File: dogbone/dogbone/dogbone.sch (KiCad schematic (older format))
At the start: 11 parts, among them J1 jstsh4x1, U1 TLV2771CDBVT

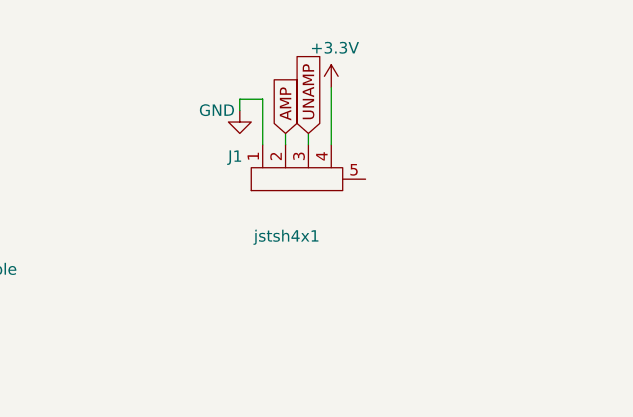
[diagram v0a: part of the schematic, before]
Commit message: added grbl files for dogbone, and update csv
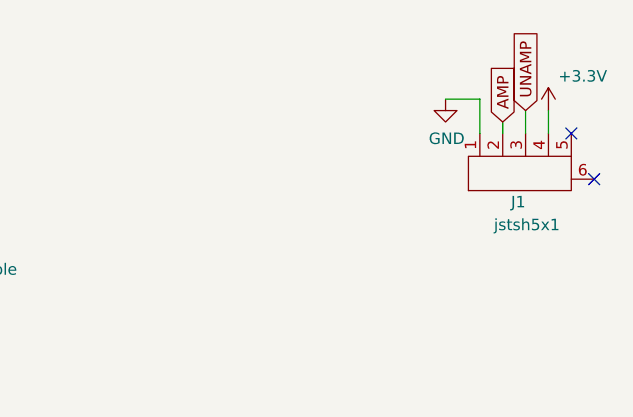
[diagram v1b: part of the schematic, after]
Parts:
- removed J1: jstsh4x1, exocam_charge_amp:jstsh4x1, symbol exocam_charge_amp:jstsh4x1
- added J1: jstsh5x1, symbol exocam_charge_amp:jstsh5x1
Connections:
- net +3V3: now also J1.4
- net AMP: now also J1.2
- net GND: now also J1.1
- net UNAMP: now also J1.3
- no-connect marks 0 -> 2
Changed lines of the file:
@@
 UNAMP
 $Comp
-L exocam_charge_amp:jstsh4x1 J1
-U 1 1 60E73D05
-P 4800 1050
-F 0 "J1" V 4849 1088 50  0000 L CNN
-F 1 "jstsh4x1" V 4500 750 50  0000 L CNN
-F 2 "exocam_charge_amp:jstsh4x1" H 4750 1200 50  0001 C CNN
-F 3 "" H 4750 1200 50  0001 C CNN
-	1    4800 1050
+L exocam_charge_amp:jstsh5x1 J1
+U 1 1 60F622D2
+P 5750 1000
+F 0 "J1" V 5550 750 50  0000 L CNN
+F 1 "jstsh5x1" V 5450 600 50  0000 L CNN
+F 2 "" H 5700 1150 50  0001 C CNN
+F 3 "" H 5700 1150 50  0001 C CNN
+	1    5750 1000
 	0    -1   -1   0
 $EndComp
 $Comp
-L power:GND #PWR0105
-U 1 1 60E75791
-P 4750 800
-F 0 "#PWR0105" H 4750 550 50  0001 C CNN
-F 1 "GND" H 4650 800 50  0000 C CNN
-F 2 "" H 4750 800 50  0001 C CNN
-F 3 "" H 4750 800 50  0001 C CNN
-	1    4750 800
+L exocam_charge_amp-cache:+3.3V #PWR?
+U 1 1 60F62E23
+P 6100 800
+F 0 "#PWR?" H 6100 650 50  0001 C CNN
+F 1 "+3.3V" H 6250 950 50  0000 C CNN
+F 2 "" H 6100 800 50  0001 C CNN
+F 3 "" H 6100 800 50  0001 C CNN
+	1    6100 800
 	1    0    0    -1
 $EndComp
-Wire Wire Line
-	4750 750  4750 800
-Wire Wire Line
-	4750 750  4850 750
-Wire Wire Line
-	4850 750  4850 950
 $Comp
-L exocam_charge_amp-cache:+3.3V #PWR0106
-U 1 1 60E76333
-P 5150 700
-F 0 "#PWR0106" H 5150 550 50  0001 C CNN
-F 1 "+3.3V" H 5165 873 50  0000 C CNN
-F 2 "" H 5150 700 50  0001 C CNN
-F 3 "" H 5150 700 50  0001 C CNN
-	1    5150 700
+L power:GND #PWR?
+U 1 1 60F633AB
+P 5650 750
+F 0 "#PWR?" H 5650 500 50  0001 C CNN
+F 1 "GND" H 5655 577 50  0000 C CNN
+F 2 "" H 5650 750 50  0001 C CNN
+F 3 "" H 5650 750 50  0001 C CNN
+	1    5650 750
 	1    0    0    -1
 $EndComp
-Wire Wire Line
-	5150 700  5150 950
-Text GLabel 4950 900  1    50   Input ~ 0
+Text GLabel 5900 850  1    50   Input ~ 0
 AMP
-Text GLabel 5050 900  1    50   Input ~ 0
+Text GLabel 6000 800  1    50   Input ~ 0
 UNAMP
 Wire Wire Line
-	4950 900  4950 950
+	5650 750  5800 750
 Wire Wire Line
-	5050 900  5050 950
+	5800 750  5800 900
+Wire Wire Line
+	5900 850  5900 900
+Wire Wire Line
+	6000 800  6000 900
+Wire Wire Line
+	6100 800  6100 900
+NoConn ~ 6200 900
+NoConn ~ 6300 1100
 $EndSCHEMATC

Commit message: updated dog bone schematic
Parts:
- J1: footprint (none) -> exocam_charge_amp:jstsh5x1
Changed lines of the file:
@@
 F 0 "J1" V 5550 750 50  0000 L CNN
 F 1 "jstsh5x1" V 5450 600 50  0000 L CNN
-F 2 "" H 5700 1150 50  0001 C CNN
+F 2 "exocam_charge_amp:jstsh5x1" H 5700 1150 50  0001 C CNN
 F 3 "" H 5700 1150 50  0001 C CNN
 	1    5750 1000
@@
 $EndComp
 $Comp
-L exocam_charge_amp-cache:+3.3V #PWR?
+L exocam_charge_amp-cache:+3.3V #PWR0105
 U 1 1 60F62E23
 P 6100 800
-F 0 "#PWR?" H 6100 650 50  0001 C CNN
+F 0 "#PWR0105" H 6100 650 50  0001 C CNN
 F 1 "+3.3V" H 6250 950 50  0000 C CNN
 F 2 "" H 6100 800 50  0001 C CNN
@@
 $EndComp
 $Comp
-L power:GND #PWR?
+L power:GND #PWR0106
 U 1 1 60F633AB
 P 5650 750
-F 0 "#PWR?" H 5650 500 50  0001 C CNN
+F 0 "#PWR0106" H 5650 500 50  0001 C CNN
 F 1 "GND" H 5655 577 50  0000 C CNN
 F 2 "" H 5650 750 50  0001 C CNN
